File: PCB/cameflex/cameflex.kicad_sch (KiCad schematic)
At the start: 44 parts, among them J1 ESP32-C3_Left, J2 ESP32-C3_Right, J3 CON5_HALL, Q1 JY317P, Q2 JY2605, Q3 JY2605, Q4 JY2605, U1 JY01(8559), U3 JY213L

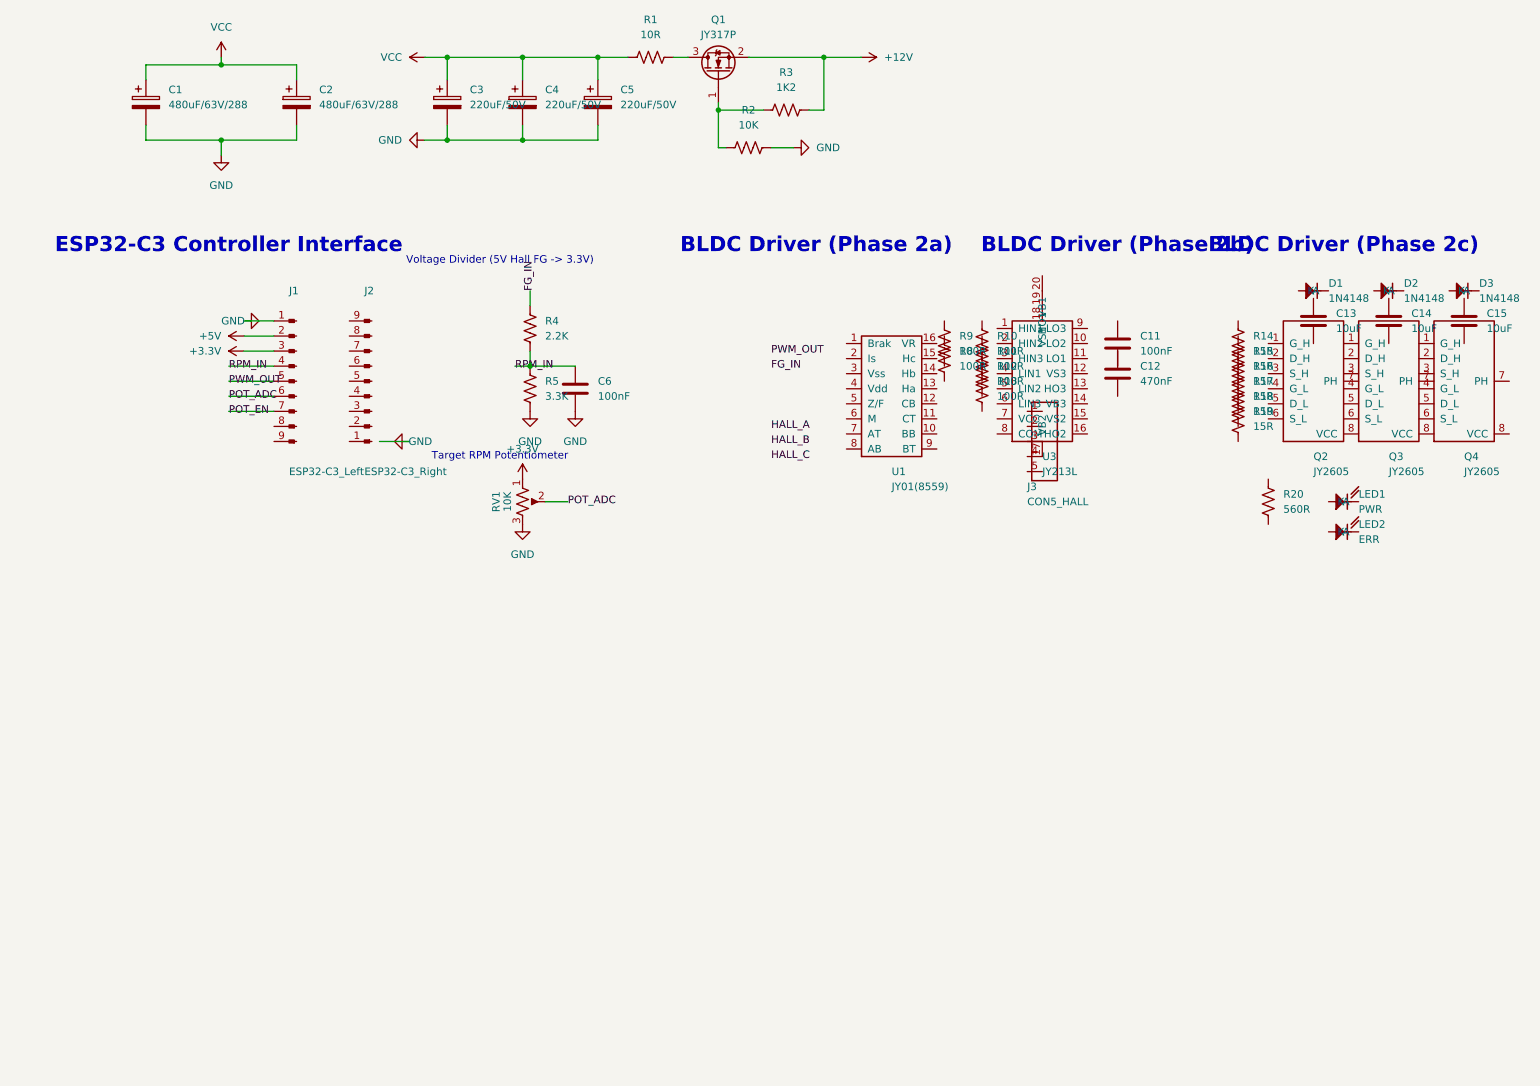
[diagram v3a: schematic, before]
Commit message: Refactor Arduino Uno PID control and sensitivity trim integration
- Updated the PID control logic to allow for a sensitivity trim via a potentiometer, enhancing tuning flexibility without altering the target RPM.
- Removed obsolete potentiometer handling for target RPM and replaced it with a single sensitivity scale adjustment.
- Simplified the control loop by consolidating mode checks and updating gain calculations based on the sensitivity trim.
- Revised documentation to reflect changes in hardware setup and configuration for improved clarity and usability.
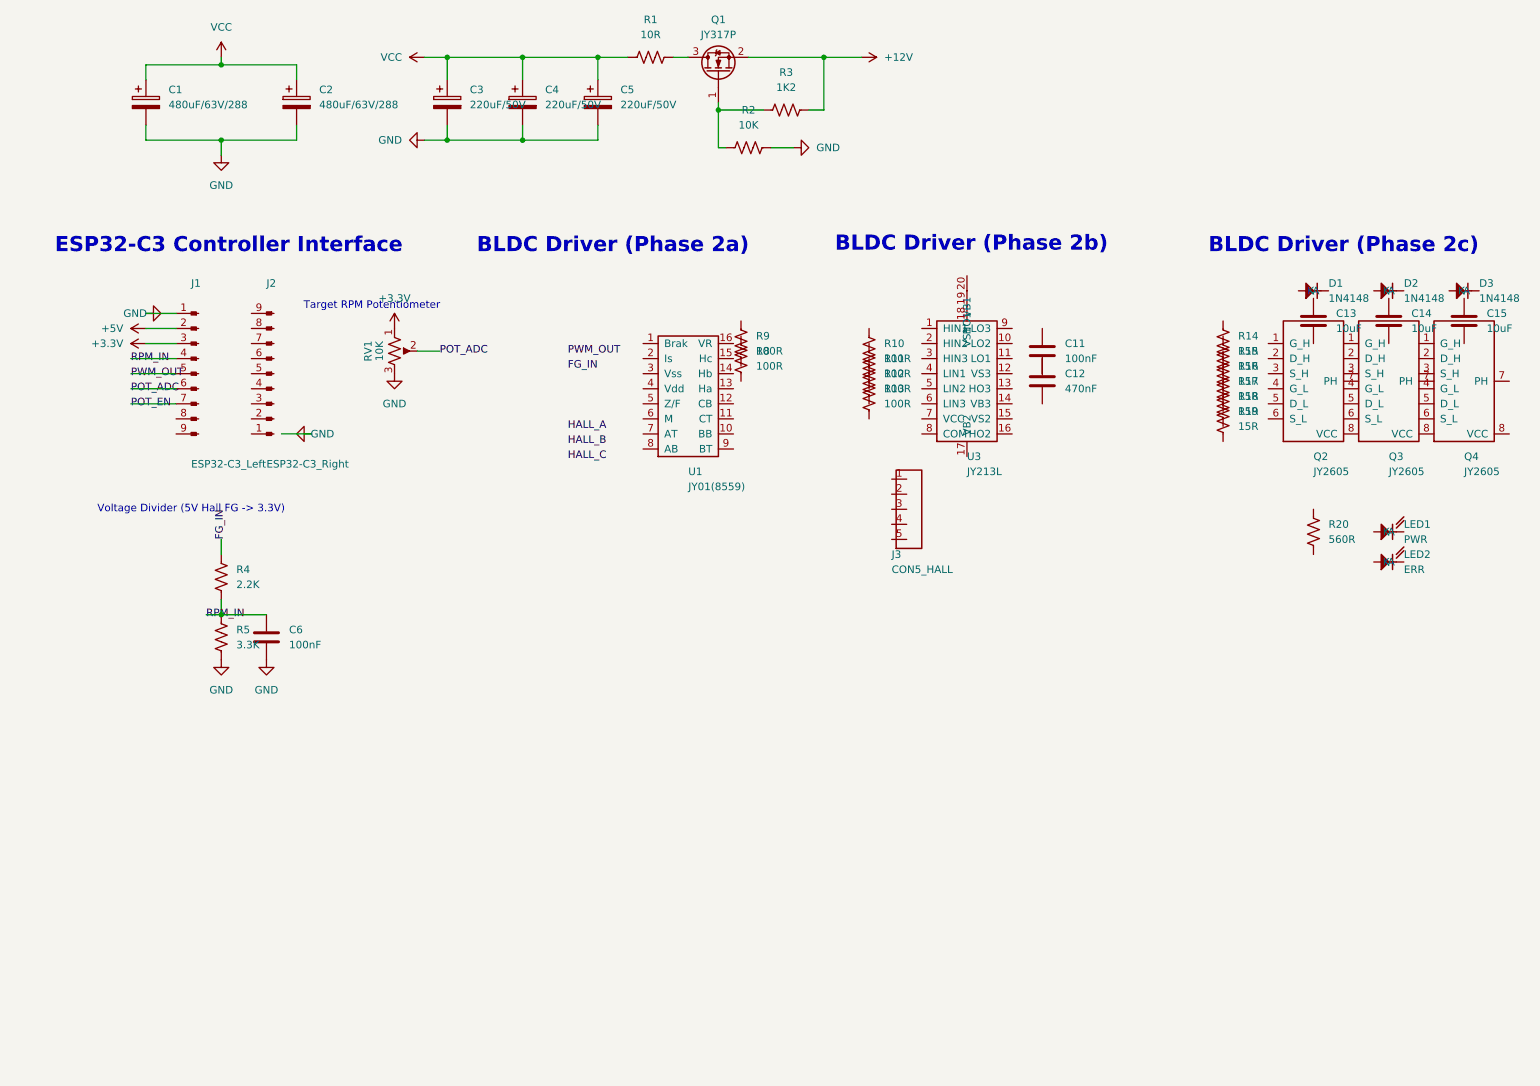
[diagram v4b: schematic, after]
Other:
- moved on the sheet: C11, C12, C6, J1, J2, J3, LED1, LED2, R10, R11, R12, R13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
